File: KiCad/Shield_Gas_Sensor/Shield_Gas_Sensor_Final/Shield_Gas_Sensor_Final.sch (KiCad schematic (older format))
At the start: 20 parts, among them P1 Power, P2 Analog, P3 Digital, P4 Digital, P5 CONN_01X01, P6 CONN_01X01, P7 CONN_01X01, P8 CONN_01X01, U1 LTC1050ACN8#PBF, U2 Gas_Sensor_TO-5, U3 RN2483_Breakout

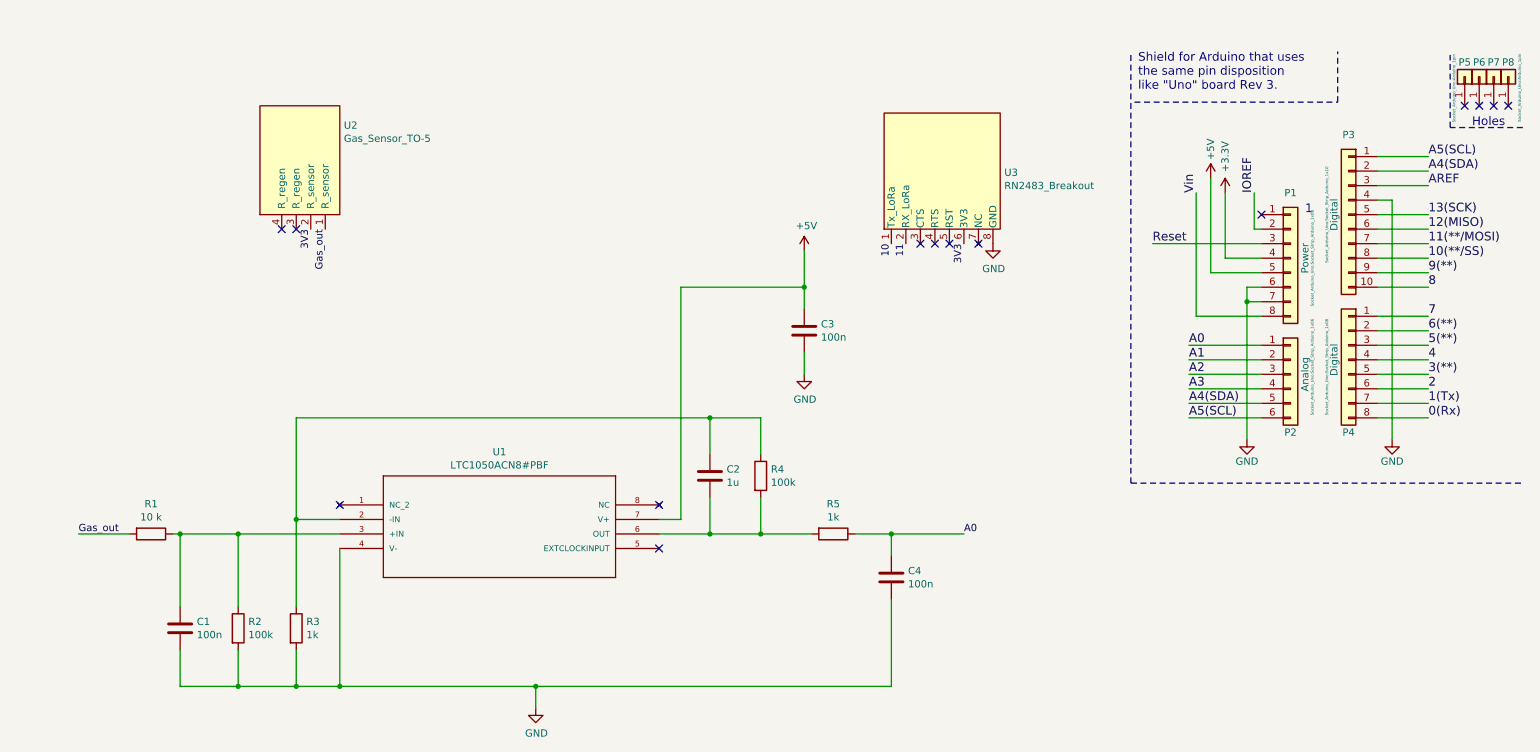
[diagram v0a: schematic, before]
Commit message: Correction Tx/Rx and Screens
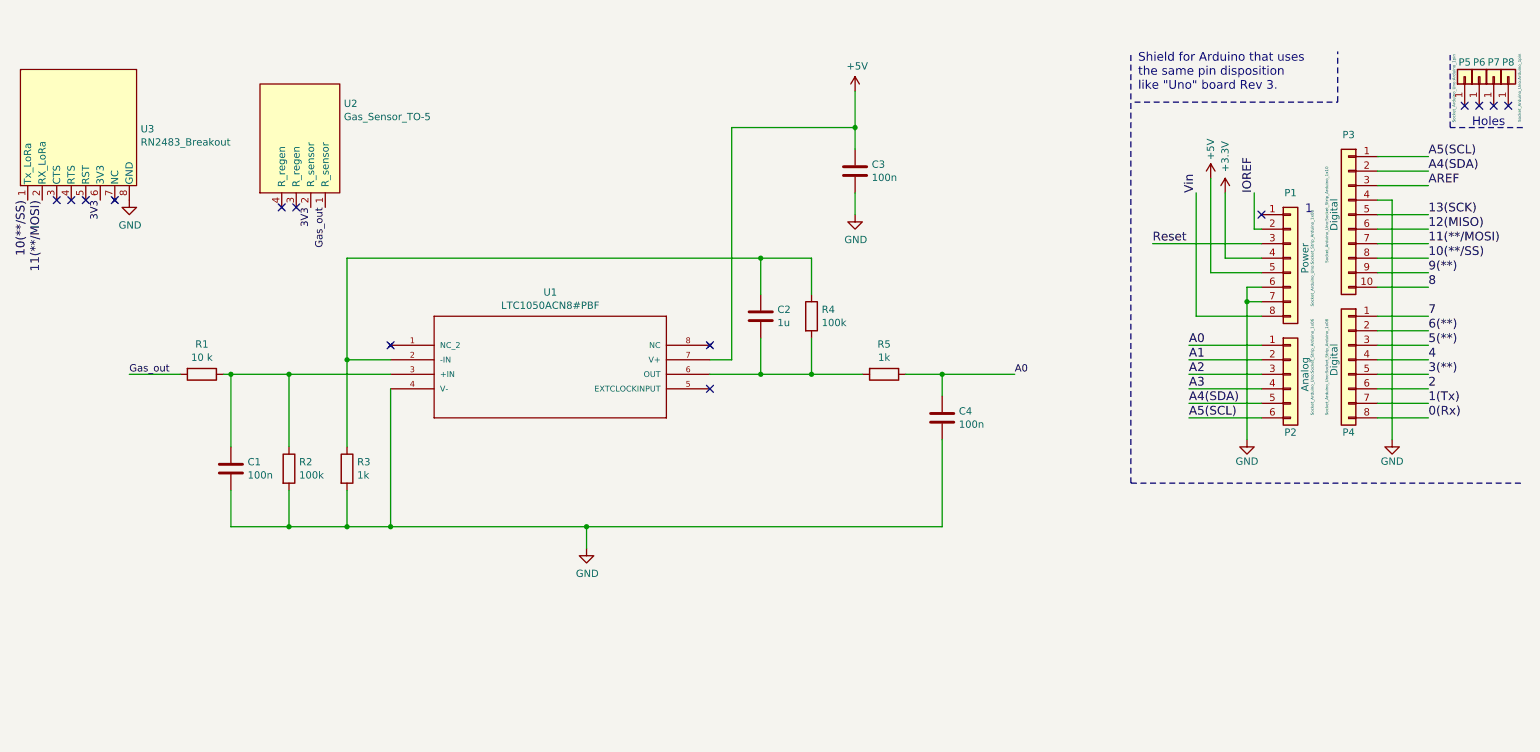
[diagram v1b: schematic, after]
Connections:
- net 10 is gone; now on net 10(**/SS): U3.1 (Tx_LoRa)
- net 11 is gone; now on net 11(**/MOSI): U3.2 (RX_LoRa)
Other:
- moved on the sheet: C1, C2, C3, C4, R1, R2, R3, R4, R5, U1, U2, U3
